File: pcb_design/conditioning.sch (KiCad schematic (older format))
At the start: 41 parts, among them U3 OPA2376AID, U4 LM2903-SO8

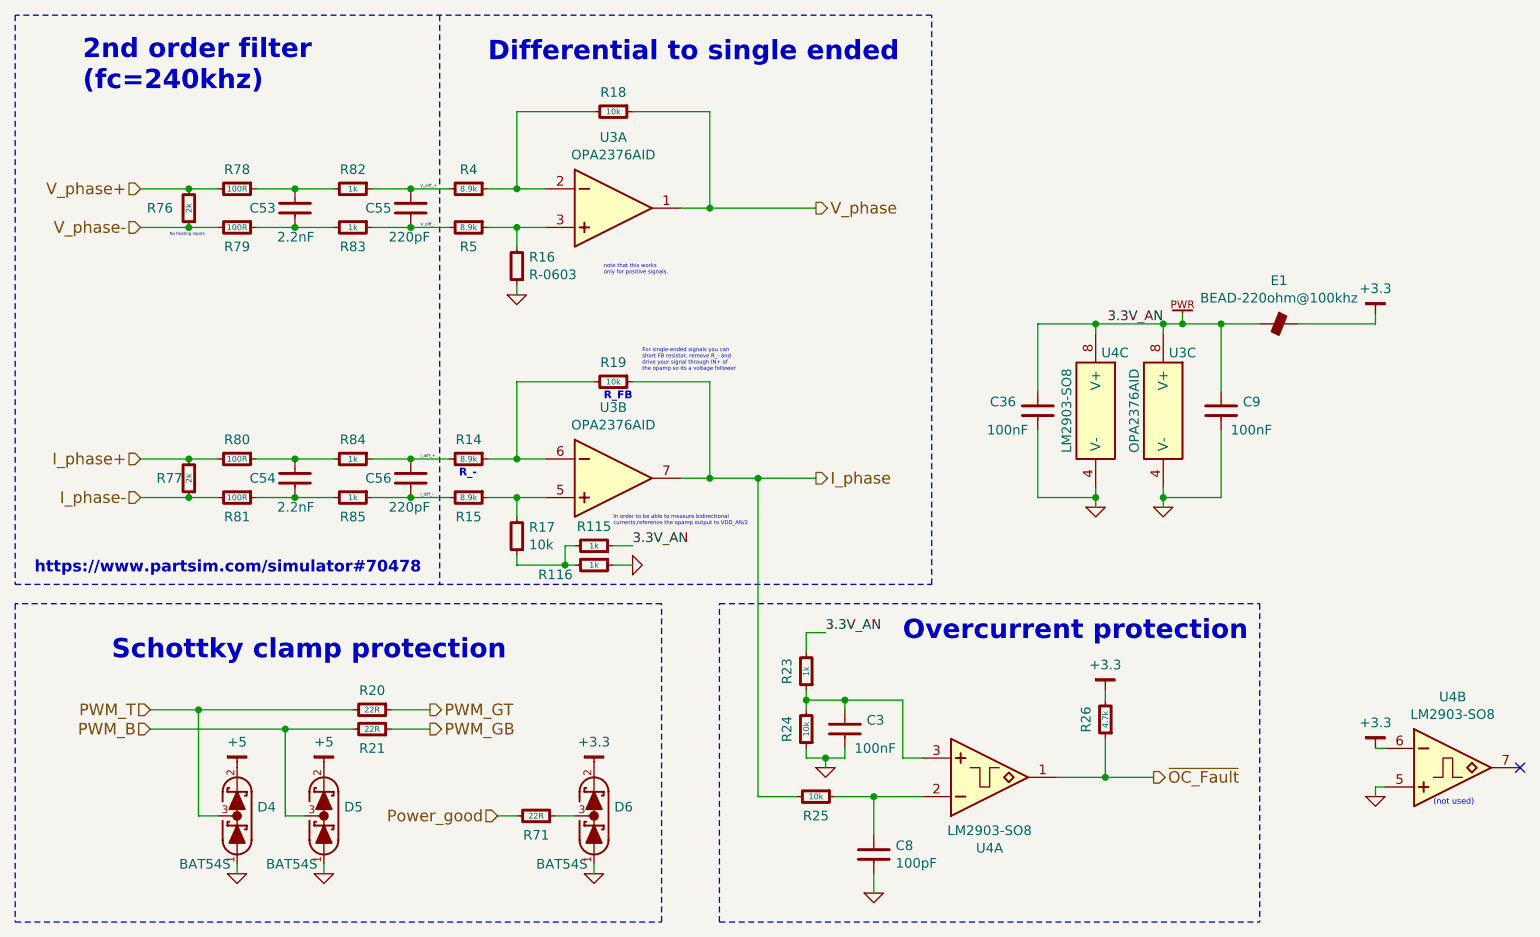
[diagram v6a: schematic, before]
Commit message: Completed part number, manufacturer, etc fields. Simulated analog conditioning
Signed-off-by: Marcos Chaparro <mchaparro@paltatech.com>
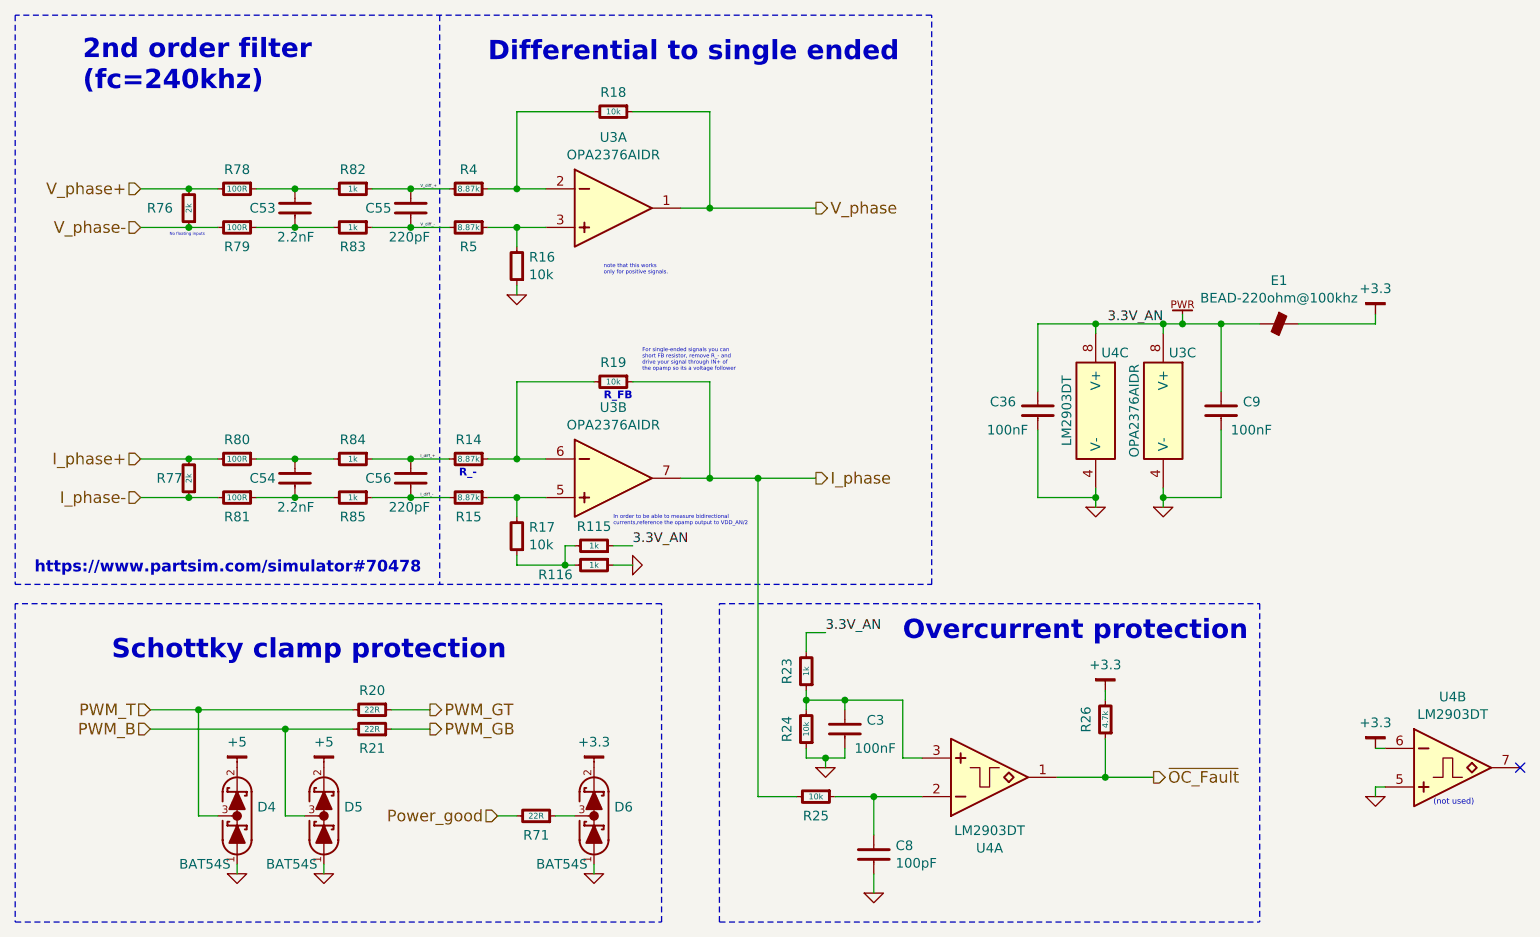
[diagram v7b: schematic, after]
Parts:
- D4, D5, D6: MFR (none) -> Toshiba Semiconductor and Storage; MPN (none) -> TBAT54S,LM; SPN (none) -> TBAT54SLMCT-ND; SPR (none) -> Digikey
- E1: MFR (none) -> Murata Electronics North America; MPN (none) -> BLM21PG221SN1D; SPN (none) -> 490-1054-1-ND; SPR (none) -> Digikey
- R115, R116, R23, R82, R83, R84, R85: MFR (none) -> Yageo; MPN (none) -> RC0603FR-071KL; SPN (none) -> 311-1.00KHRCT-ND; SPR (none) -> Digikey
- R14, R15, R4, R5: value 8.9k -> 8.87k; MFR (none) -> Yageo; MPN (none) -> RC0603FR-078K87L; SPN (none) -> 311-8.87KHRCT-ND; SPR (none) -> Digikey
- R16: value R-0603 -> 10k
- R17, R18, R19, R24, R25: MFR (none) -> Yageo; MPN (none) -> RC0603FR-0710KL; SPN (none) -> 311-10.0KHRCT-ND; SPR (none) -> Digikey
- R20, R21, R71: MFR (none) -> Yageo; MPN (none) -> RC0603FR-0722RL; SPN (none) -> 311-22.0HRCT-ND; SPR (none) -> Digikey
- R26: MFR (none) -> Yageo; MPN (none) -> RC0603FR-074K7L; SPN (none) -> 311-4.70KHRCT-ND; SPR (none) -> Digikey
- R76, R77: MFR (none) -> Yageo; MPN (none) -> RC0603FR-072KL; SPN (none) -> 311-2.00KHRCT-ND; SPR (none) -> Digikey
- R78, R79, R80, R81: MFR (none) -> Yageo; MPN (none) -> RC0603FR-07100RL; SPN (none) -> 311-100HRCT-ND; SPR (none) -> Digikey
- U3: value OPA2376AID -> OPA2376AIDR; MFR (none) -> Texas Instruments; MPN (none) -> OPA2376AIDR; SPN (none) -> 296-22564-1-ND; SPR (none) -> Digikey
- U4: value LM2903-SO8 -> LM2903DT; MFR (none) -> STMicroelectronics; MPN (none) -> LM2903DT; SPN (none) -> 497-1559-1-ND; SPR (none) -> Digikey

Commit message: Corrected phase current gain. More 3d models
Signed-off-by: Marcos Chaparro <mchaparro@paltatech.com>
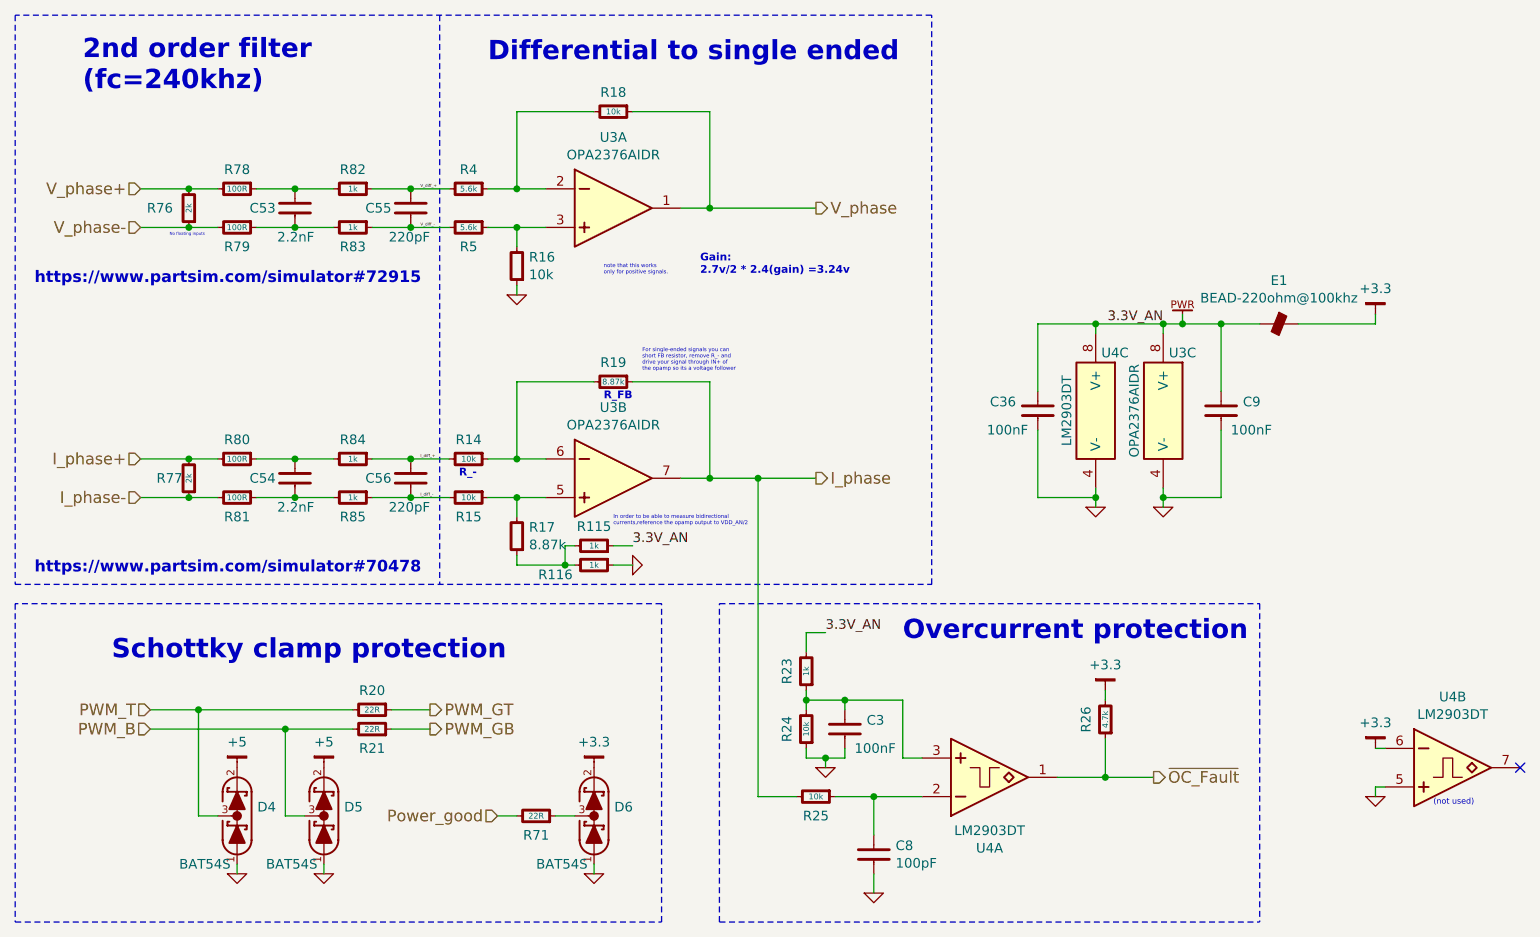
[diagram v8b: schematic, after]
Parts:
- E1: mfg# BLM21PG221SN1D -> (none)
- R14, R15: value 8.87k -> 10k
- R17, R19: value 10k -> 8.87k
- R4, R5: value 8.87k -> 5.6k
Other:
- note added: "Gain:\n2.7v/2 * 2.4(gain) =3.24v"
- note added: "https://www.partsim.com/simulator#72915"
